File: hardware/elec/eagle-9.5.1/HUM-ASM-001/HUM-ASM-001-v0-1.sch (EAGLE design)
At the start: 4 parts

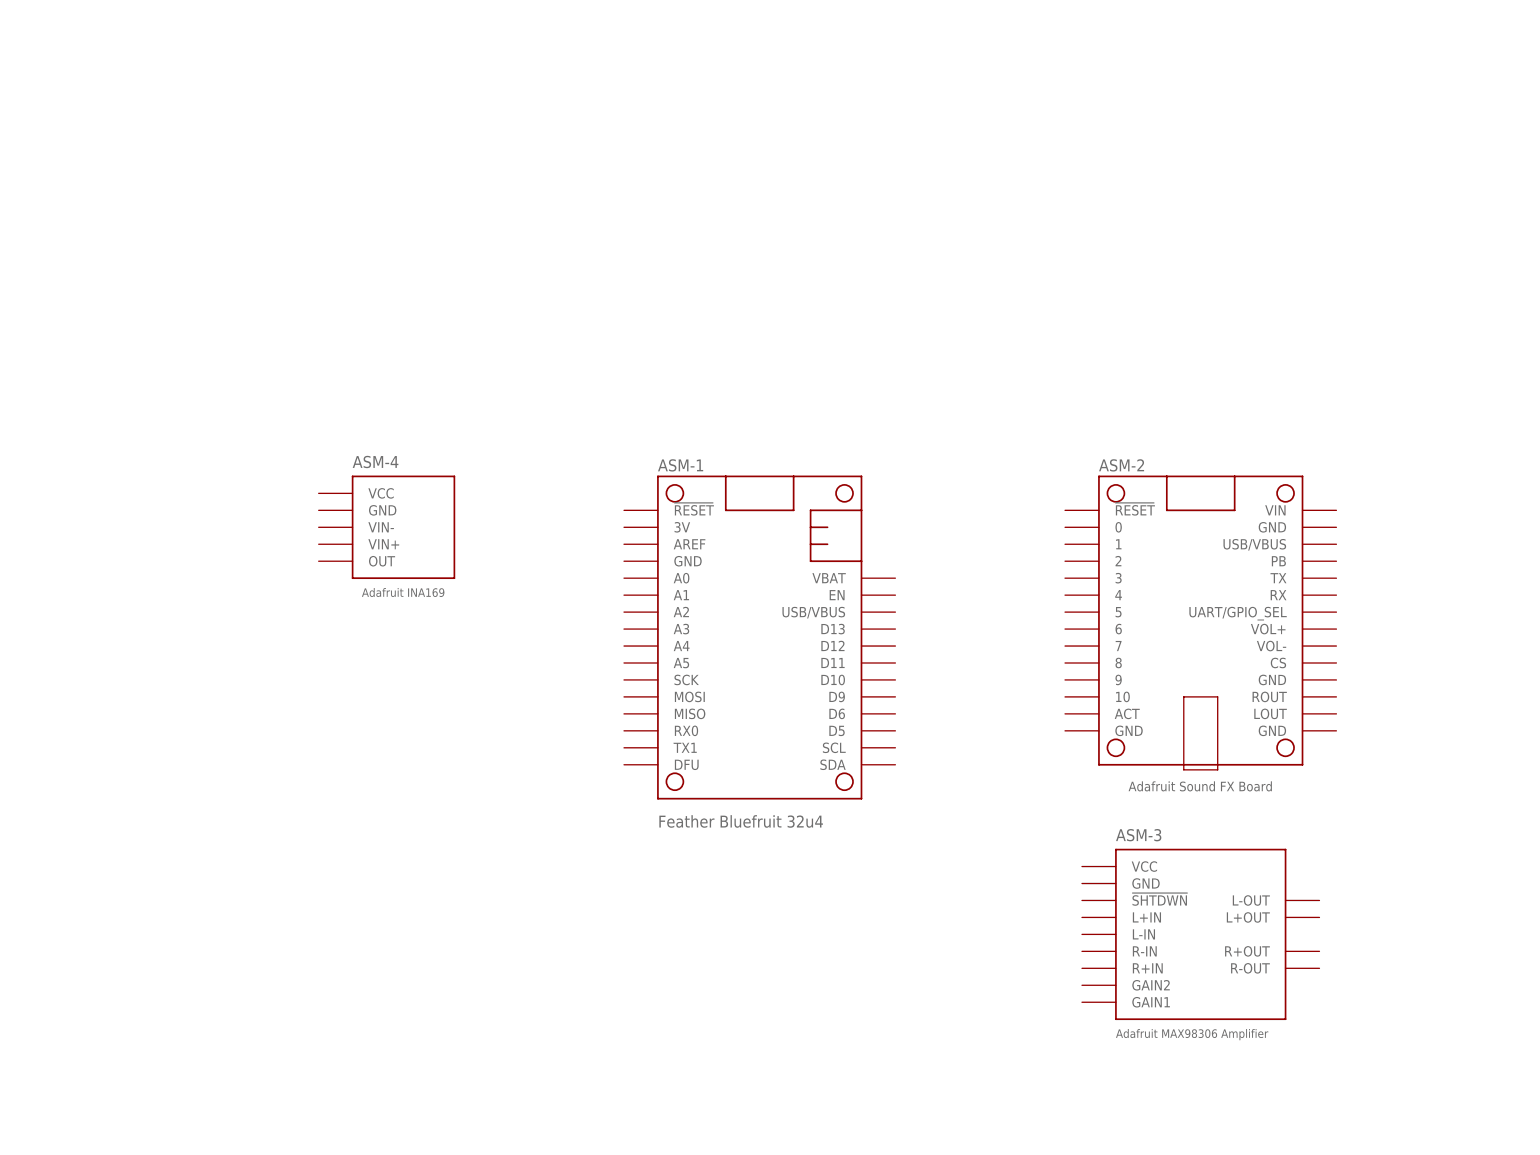
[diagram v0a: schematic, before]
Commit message: * added more footprints to library and parts to schematic
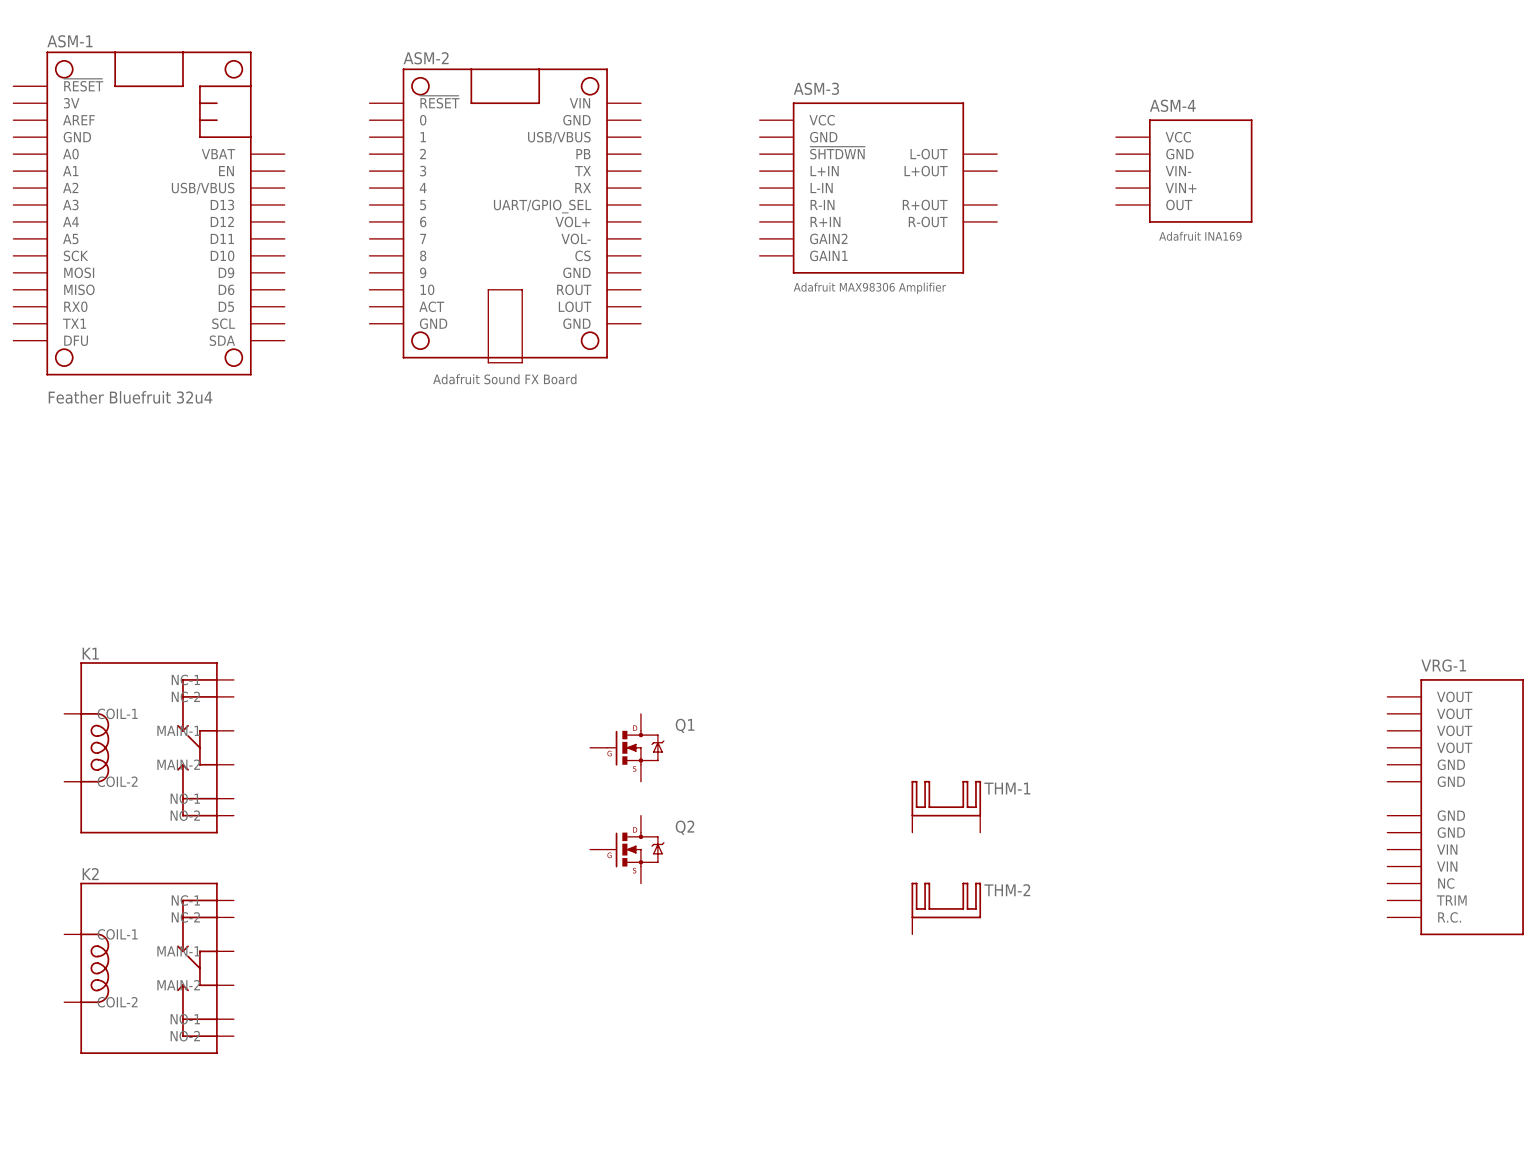
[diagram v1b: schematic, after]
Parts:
- added K1, K2: (no value), MG-Eagle_v1:EMD_RELAY_SPDT_8-PIN_TE_7-1393239-7
- added Q1, Q2: (no value), MG-Eagle_v1:TRN_MOSFET-N_TO-220_VERTICAL
- added THM-1: (no value), MG-Eagle_v1:THM_HEATSINK_2-PIN
- added THM-2: (no value), MG-Eagle_v1:THM_HEATSINK_1-PIN
- added VRG-1: (no value), MG-Eagle_v1:VRG_NID100
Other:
- moved on the sheet: ASM-1, ASM-2, ASM-3, ASM-4
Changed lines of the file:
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@@
 <layer number="96" name="Values" color="7" fill="1" visible="yes" active="yes"/>
 <layer number="97" name="Info" color="15" fill="1" visible="yes" active="yes"/>
+<layer number="200" name="BMP_1" color="1" fill="1" visible="yes" active="yes"/>
+<layer number="201" name="BMP_2" color="1" fill="1" visible="yes" active="yes"/>
 <layer number="99" name="SpiceOrder" color="7" fill="1" visible="no" active="no"/>
 <layer number="100" name="Muster" color="7" fill="1" visible="no" active="no"/>
@@
 <layer number="155" name="FabDoc3" color="7" fill="15" visible="no" active="no"/>
 <layer number="199" name="Contour" color="7" fill="1" visible="no" active="no"/>
-<layer number="200" name="BMP_1" color="1" fill="1" visible="yes" active="yes"/>
-<layer number="201" name="BMP_2" color="1" fill="1" visible="yes" active="yes"/>
 <layer number="1" name="Top" color="12" fill="1" visible="no" active="no"/>
 <layer number="2" name="Route2" color="1" fill="4" visible="no" active="no"/>
@@
 <part name="ASM-3" library="MG-Eagle_v1" deviceset="ASM_ADAFRUIT_MAX98306_AMP" device=""/>
 <part name="ASM-4" library="MG-Eagle_v1" deviceset="ASM_ADAFRUIT_INA169" device=""/>
+<part name="VRG-1" library="MG-Eagle_v1" deviceset="VRG_NID100" device=""/>
+<part name="K1" library="MG-Eagle_v1" deviceset="EMD_RELAY_SPDT_8-PIN" device="_TE_7-1393239-7"/>
+<part name="K2" library="MG-Eagle_v1" deviceset="EMD_RELAY_SPDT_8-PIN" device="_TE_7-1393239-7"/>
+<part name="Q1" library="MG-Eagle_v1" deviceset="TRN_MOSFET-N" device="_TO-220_VERTICAL"/>
+<part name="Q2" library="MG-Eagle_v1" deviceset="TRN_MOSFET-N" device="_TO-220_VERTICAL"/>
+<part name="THM-1" library="MG-Eagle_v1" deviceset="THM_HEATSINK_2-PIN" device=""/>
+<part name="THM-2" library="MG-Eagle_v1" deviceset="THM_HEATSINK_1-PIN" device="" package3d_urn="urn:adsk.eagle:package:14183/1"/>
 </parts>
 <sheets>
@@
 <attribute name="DESIGNER" x="217.37" y="-187.96" size="2.54" layer="94" font="vector"/>
 </instance>
-<instance part="ASM-1" gate="G$1" x="124.46" y="-104.14" smashed="yes">
-<attribute name="NAME" x="109.22" y="-73.66" size="1.778" layer="95" align="top-left"/>
-<attribute name="VALUE" x="109.22" y="-127" size="1.778" layer="96" align="top-left"/>
-</instance>
-<instance part="ASM-2" gate="G$1" x="190.5" y="-104.14" smashed="yes">
-<attribute name="NAME" x="175.26" y="-73.66" size="1.778" layer="95" align="top-left"/>
-</instance>
-<instance part="ASM-3" gate="G$1" x="190.5" y="-144.78" smashed="yes">
-<attribute name="NAME" x="177.8" y="-130.81" size="1.778" layer="95" font="vector"/>
-</instance>
-<instance part="ASM-4" gate="G$1" x="71.12" y="-83.82" smashed="yes">
-<attribute name="NAME" x="63.5" y="-74.93" size="1.778" layer="95" font="vector"/>
+<instance part="ASM-1" gate="G$1" x="33.02" y="-40.64" smashed="yes">
+<attribute name="NAME" x="17.78" y="-10.16" size="1.778" layer="95" align="top-left"/>
+<attribute name="VALUE" x="17.78" y="-63.5" size="1.778" layer="96" align="top-left"/>
+</instance>
+<instance part="ASM-2" gate="G$1" x="86.36" y="-43.18" smashed="yes">
+<attribute name="NAME" x="71.12" y="-12.7" size="1.778" layer="95" align="top-left"/>
+</instance>
+<instance part="ASM-3" gate="G$1" x="142.24" y="-33.02" smashed="yes">
+<attribute name="NAME" x="129.54" y="-19.05" size="1.778" layer="95" font="vector"/>
+</instance>
+<instance part="ASM-4" gate="G$1" x="190.5" y="-30.48" smashed="yes">
+<attribute name="NAME" x="182.88" y="-21.59" size="1.778" layer="95" font="vector"/>
+</instance>
+<instance part="VRG-1" gate="G$1" x="231.14" y="-124.46" smashed="yes">
+<attribute name="VALUE" x="223.52" y="-146.304" size="1.27" layer="96" font="vector" align="top-left"/>
+<attribute name="NAME" x="223.52" y="-105.41" size="1.778" layer="95" font="vector"/>
+</instance>
+<instance part="K1" gate="G$1" x="33.02" y="-116.84" smashed="yes">
+<attribute name="NAME" x="22.86" y="-103.632" size="1.778" layer="95"/>
+<attribute name="VALUE" x="22.86" y="-132.08" size="1.778" layer="96"/>
+</instance>
+<instance part="K2" gate="G$1" x="33.02" y="-149.86" smashed="yes">
+<attribute name="NAME" x="22.86" y="-136.652" size="1.778" layer="95"/>
+<attribute name="VALUE" x="22.86" y="-165.1" size="1.778" layer="96"/>
+</instance>
+<instance part="Q1" gate="G$1" x="106.68" y="-116.84" smashed="yes">
+<attribute name="NAME" x="111.76" y="-114.3" size="1.778" layer="95" font="vector"/>
+<attribute name="VALUE" x="111.76" y="-116.84" size="1.27" layer="96" font="vector" ratio="12"/>
+</instance>
+<instance part="Q2" gate="G$1" x="106.68" y="-132.08" smashed="yes">
+<attribute name="NAME" x="111.76" y="-129.54" size="1.778" layer="95" font="vector"/>
+<attribute name="VALUE" x="111.76" y="-132.08" size="1.27" layer="96" font="vector" ratio="12"/>
+</instance>
+<instance part="THM-1" gate="G$1" x="152.4" y="-127" smashed="yes">
+<attribute name="NAME" x="158.115" y="-123.825" size="1.778" layer="95"/>
+<attribute name="VALUE" x="158.115" y="-126.365" size="1.778" layer="96"/>
+</instance>
+<instance part="THM-2" gate="G$1" x="152.4" y="-142.24" smashed="yes">
+<attribute name="NAME" x="158.115" y="-139.065" size="1.778" layer="95"/>
+<attribute name="VALUE" x="158.115" y="-141.605" size="1.778" layer="96"/>
 </instance>
 </instances>
@@
 which will not be processed correctly with this version.
 </note>
+<note version="8.3" severity="warning">
+Since Version 8.3, EAGLE supports URNs for individual library
+assets (packages, symbols, and devices). The URNs of those assets
+will not be understood (or retained) with this version.
+</note>
+<note version="8.3" severity="warning">
+Since Version 8.3, EAGLE supports the association of 3D packages
+with devices in libraries, schematics, and board files. Those 3D
+packages will not be understood (or retained) with this version.
+</note>
 </compatibility>
